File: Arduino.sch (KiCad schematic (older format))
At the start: 19 parts

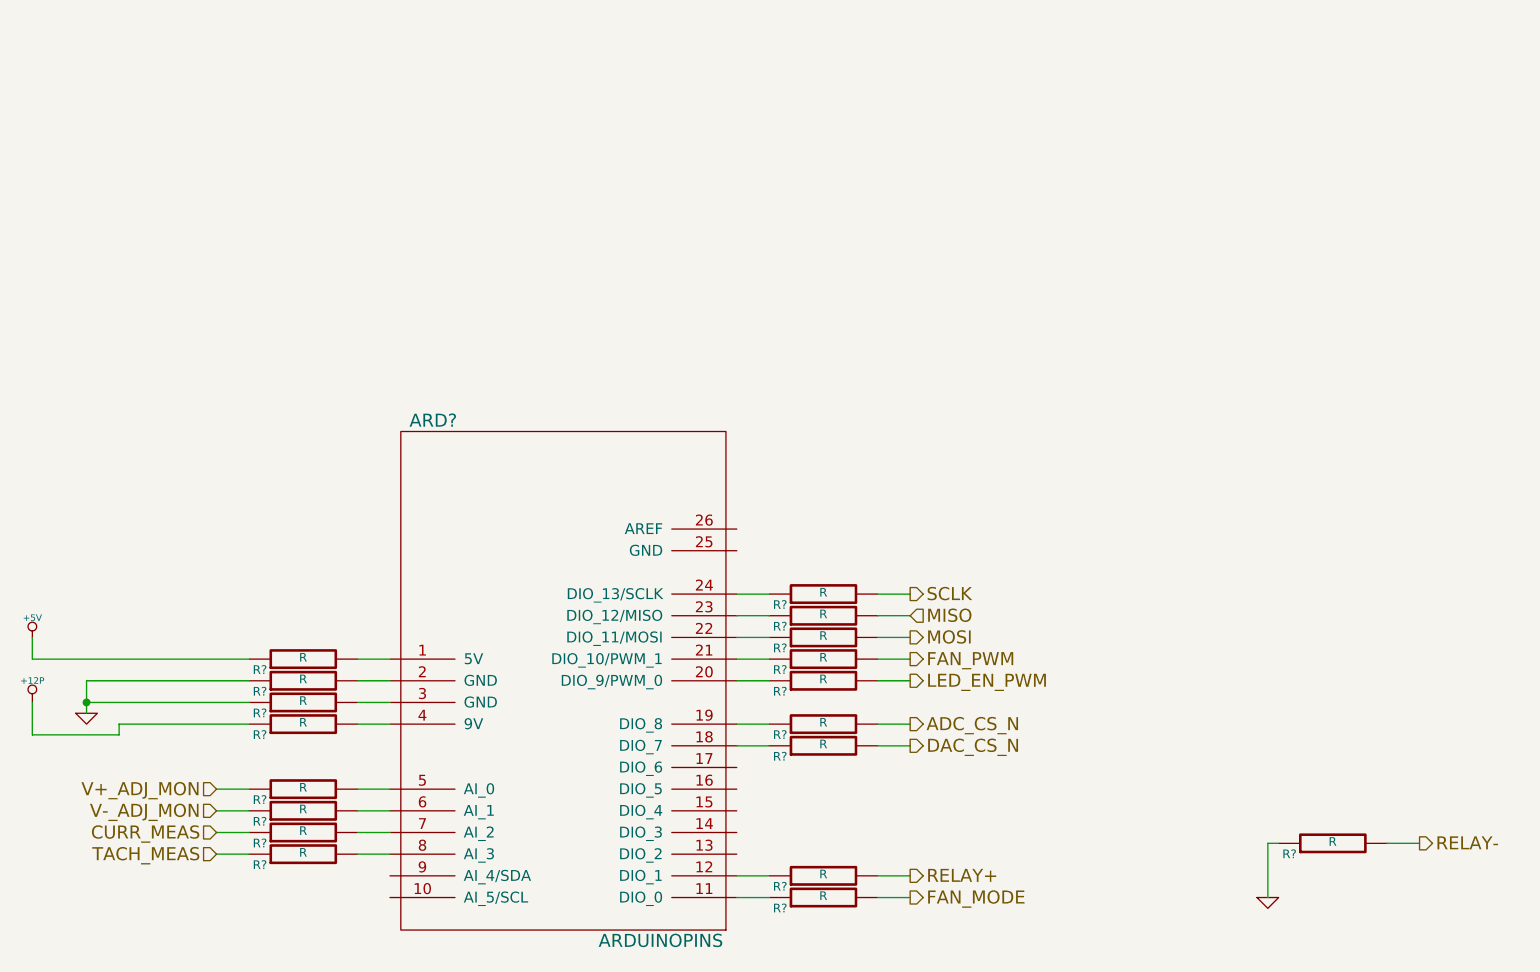
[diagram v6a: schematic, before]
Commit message: started associating relay parts
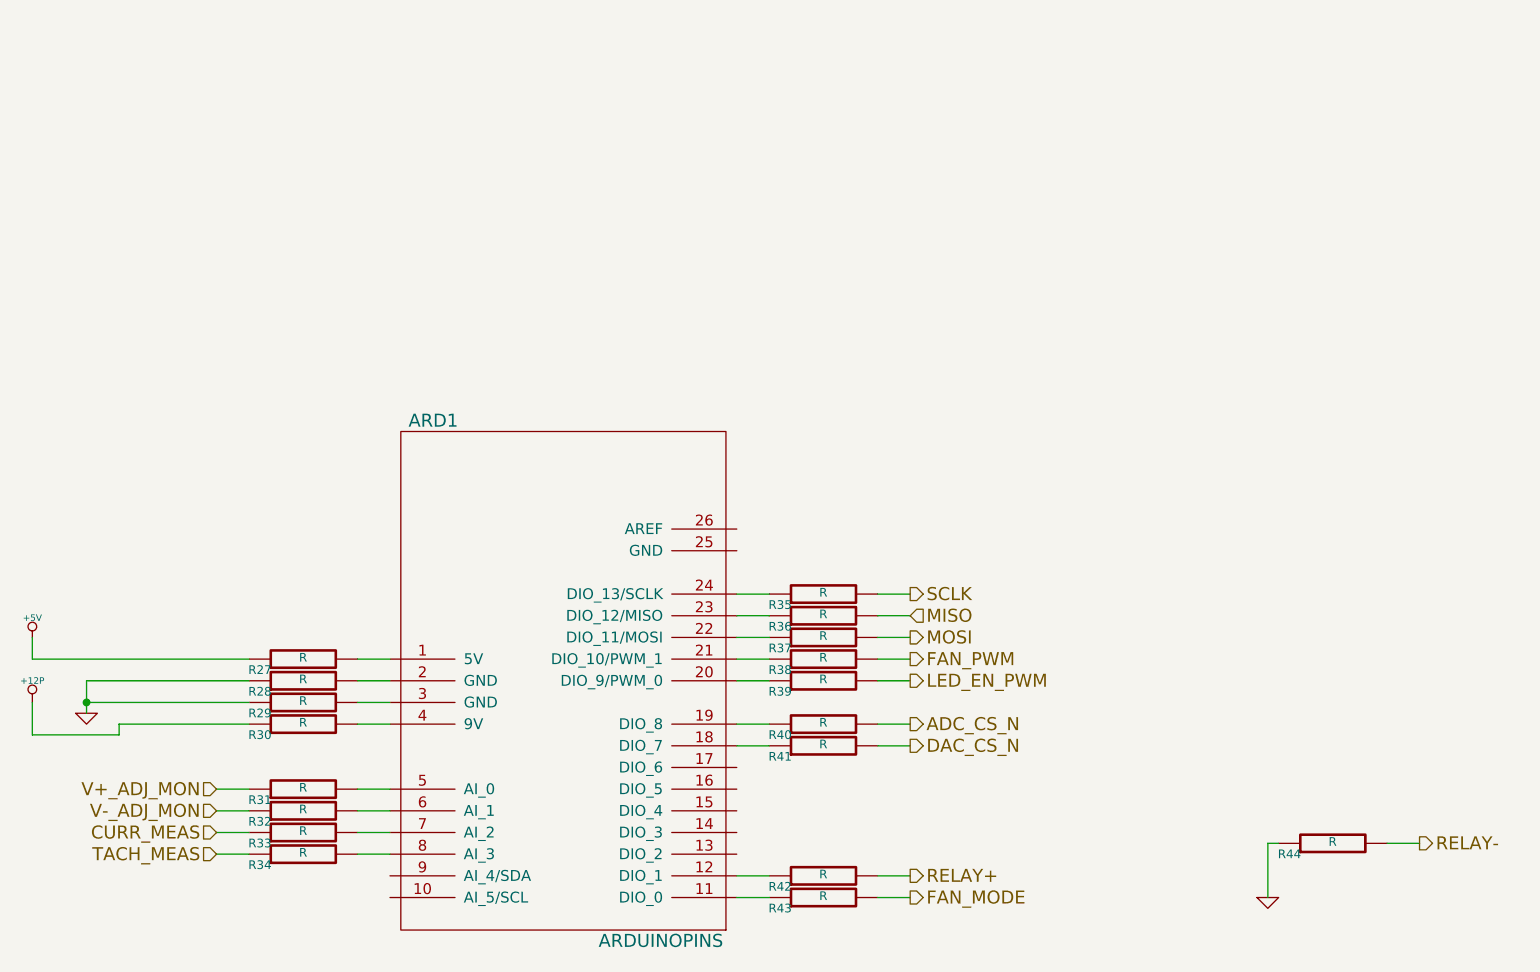
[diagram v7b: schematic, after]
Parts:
- gave numbers to parts that had none: 19
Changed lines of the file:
@@
 Sheet 9 9
 Title ""
-Date "17 feb 2014"
+Date "20 feb 2014"
 Rev ""
 Comp ""
@@
 CURR_MEAS
 $Comp
-L R R?
+L R R38
 U 1 1 52F9D91F
 P 6000 4300
-F 0 "R?" V 5950 4500 40  0000 C CNN
+F 0 "R38" V 5950 4500 40  0000 C CNN
 F 1 "R" V 6007 4301 40  0000 C CNN
 F 2 "~" V 5930 4300 30  0000 C CNN
@@
 $EndComp
 $Comp
-L R R?
+L R R42
 U 1 1 52F9E47A
 P 6000 5300
-F 0 "R?" V 5950 5500 40  0000 C CNN
+F 0 "R42" V 5950 5500 40  0000 C CNN
 F 1 "R" V 6007 5301 40  0000 C CNN
 F 2 "~" V 5930 5300 30  0000 C CNN
@@
 	5750 5300 5600 5300
 $Comp
-L GND #PWR?
+L GND #PWR049
 U 1 1 52F9E495
 P 8050 5400
-F 0 "#PWR?" H 8050 5400 30  0001 C CNN
+F 0 "#PWR049" H 8050 5400 30  0001 C CNN
 F 1 "GND" H 8050 5330 30  0001 C CNN
 F 2 "" H 8050 5400 60  0000 C CNN
@@
 $EndComp
 $Comp
-L R R?
+L R R34
 U 1 1 52FA0A84
 P 3600 5200
-F 0 "R?" V 3550 5400 40  0000 C CNN
+F 0 "R34" V 3550 5400 40  0000 C CNN
 F 1 "R" V 3607 5201 40  0000 C CNN
 F 2 "~" V 3530 5200 30  0000 C CNN
@@
 $EndComp
 $Comp
-L R R?
+L R R33
 U 1 1 52FA0A8A
 P 3600 5100
-F 0 "R?" V 3550 5300 40  0000 C CNN
+F 0 "R33" V 3550 5300 40  0000 C CNN
 F 1 "R" V 3607 5101 40  0000 C CNN
 F 2 "~" V 3530 5100 30  0000 C CNN
@@
 V-_ADJ_MON
 $Comp
-L R R?
+L R R32
 U 1 1 52FA4D64
 P 3600 5000
-F 0 "R?" V 3550 5200 40  0000 C CNN
+F 0 "R32" V 3550 5200 40  0000 C CNN
 F 1 "R" V 3607 5001 40  0000 C CNN
 F 2 "~" V 3530 5000 30  0000 C CNN
@@
 $EndComp
 $Comp
-L R R?
+L R R31
 U 1 1 52FA4D6A
 P 3600 4900
-F 0 "R?" V 3550 5100 40  0000 C CNN
+F 0 "R31" V 3550 5100 40  0000 C CNN
 F 1 "R" V 3607 4901 40  0000 C CNN
 F 2 "~" V 3530 4900 30  0000 C CNN
@@
 	3850 4900 4000 4900
 $Comp
-L R R?
+L R R44
 U 1 1 52FA5DED
 P 8350 5150
-F 0 "R?" V 8300 5350 40  0000 C CNN
+F 0 "R44" V 8300 5350 40  0000 C CNN
 F 1 "R" V 8357 5151 40  0000 C CNN
 F 2 "~" V 8280 5150 30  0000 C CNN
@@
 	8600 5150 8750 5150
 $Comp
-L R R?
+L R R41
 U 1 1 52FA6082
 P 6000 4700
-F 0 "R?" V 5950 4900 40  0000 C CNN
+F 0 "R41" V 5950 4900 40  0000 C CNN
 F 1 "R" V 6007 4701 40  0000 C CNN
 F 2 "~" V 5930 4700 30  0000 C CNN
@@
 $EndComp
 $Comp
-L R R?
+L R R37
 U 1 1 52FA6088
 P 6000 4200
-F 0 "R?" V 5950 4400 40  0000 C CNN
+F 0 "R37" V 5950 4400 40  0000 C CNN
 F 1 "R" V 6007 4201 40  0000 C CNN
 F 2 "~" V 5930 4200 30  0000 C CNN
@@
 $EndComp
 $Comp
-L R R?
+L R R36
 U 1 1 52FA608E
 P 6000 4100
-F 0 "R?" V 5950 4300 40  0000 C CNN
+F 0 "R36" V 5950 4300 40  0000 C CNN
 F 1 "R" V 6007 4101 40  0000 C CNN
 F 2 "~" V 5930 4100 30  0000 C CNN
@@
 $EndComp
 $Comp
-L R R?
+L R R35
 U 1 1 52FA6094
 P 6000 4000
-F 0 "R?" V 5950 4200 40  0000 C CNN
+F 0 "R35" V 5950 4200 40  0000 C CNN
 F 1 "R" V 6007 4001 40  0000 C CNN
 F 2 "~" V 5930 4000 30  0000 C CNN
@@
 LED_EN_PWM
 $Comp
-L R R?
+L R R39
 U 1 1 52FA63A1
 P 6000 4400
-F 0 "R?" V 5950 4600 40  0000 C CNN
+F 0 "R39" V 5950 4600 40  0000 C CNN
 F 1 "R" V 6007 4401 40  0000 C CNN
 F 2 "~" V 5930 4400 30  0000 C CNN
@@
 ADC_CS_N
 $Comp
-L R R?
+L R R40
 U 1 1 52FA944C
 P 6000 4600
-F 0 "R?" V 5950 4800 40  0000 C CNN
+F 0 "R40" V 5950 4800 40  0000 C CNN
 F 1 "R" V 6007 4601 40  0000 C CNN
 F 2 "~" V 5930 4600 30  0000 C CNN
@@
 FAN_MODE
 $Comp
-L R R?
+L R R43
 U 1 1 52FA55B0
 P 6000 5400
-F 0 "R?" V 5950 5600 40  0000 C CNN
+F 0 "R43" V 5950 5600 40  0000 C CNN
 F 1 "R" V 6007 5401 40  0000 C CNN
 F 2 "~" V 5930 5400 30  0000 C CNN
@@
 	6250 5400 6400 5400
 $Comp
-L R R?
+L R R30
 U 1 1 52FA5B06
 P 3600 4600
-F 0 "R?" V 3550 4800 40  0000 C CNN
+F 0 "R30" V 3550 4800 40  0000 C CNN
 F 1 "R" V 3607 4601 40  0000 C CNN
 F 2 "~" V 3530 4600 30  0000 C CNN
@@
 	3850 4600 4000 4600
 $Comp
-L +12P #PWR?
+L +12P #PWR050
 U 1 1 52FA5B4B
 P 2350 4500
-F 0 "#PWR?" H 2350 4470 30  0001 C CNN
+F 0 "#PWR050" H 2350 4470 30  0001 C CNN
 F 1 "+12P" H 2350 4600 30  0000 C CNN
 F 2 "" H 2350 4500 60  0000 C CNN
@@
 	2350 4500 2350 4650
 $Comp
-L ARDUINOPINS ARD?
+L ARDUINOPINS ARD1
 U 1 1 53022634
 P 6350 4700
-F 0 "ARD?" H 4200 6200 60  0000 C CNN
+F 0 "ARD1" H 4200 6200 60  0000 C CNN
 F 1 "ARDUINOPINS" H 5250 3800 60  0000 C CNN
 F 2 "~" H 6350 4700 60  0000 C CNN
@@
 $EndComp
 $Comp
-L R R?
+L R R27
 U 1 1 53023A69
 P 3600 4300
-F 0 "R?" V 3550 4500 40  0000 C CNN
+F 0 "R27" V 3550 4500 40  0000 C CNN
 F 1 "R" V 3607 4301 40  0000 C CNN
 F 2 "~" V 3530 4300 30  0000 C CNN
@@
 $EndComp
 $Comp
-L R R?
+L R R28
 U 1 1 53023A6F
 P 3600 4400
-F 0 "R?" V 3550 4600 40  0000 C CNN
+F 0 "R28" V 3550 4600 40  0000 C CNN
 F 1 "R" V 3607 4401 40  0000 C CNN
 F 2 "~" V 3530 4400 30  0000 C CNN
@@
 $EndComp
 $Comp
-L R R?
+L R R29
 U 1 1 53023A7F
 P 3600 4500
-F 0 "R?" V 3550 4700 40  0000 C CNN
+F 0 "R29" V 3550 4700 40  0000 C CNN
 F 1 "R" V 3607 4501 40  0000 C CNN
 F 2 "~" V 3530 4500 30  0000 C CNN
@@
 	3850 4300 4000 4300
 $Comp
-L +5V #PWR?
+L +5V #PWR051
 U 1 1 53023B11
 P 2350 4200
-F 0 "#PWR?" H 2350 4290 20  0001 C CNN
+F 0 "#PWR051" H 2350 4290 20  0001 C CNN
 F 1 "+5V" H 2350 4290 30  0000 C CNN
 F 2 "" H 2350 4200 60  0000 C CNN
@@
 	2350 4300 3350 4300
 $Comp
-L GND #PWR?
+L GND #PWR052
 U 1 1 53023B7D
 P 2600 4550
-F 0 "#PWR?" H 2600 4550 30  0001 C CNN
+F 0 "#PWR052" H 2600 4550 30  0001 C CNN
 F 1 "GND" H 2600 4480 30  0001 C CNN
 F 2 "" H 2600 4550 60  0000 C CNN

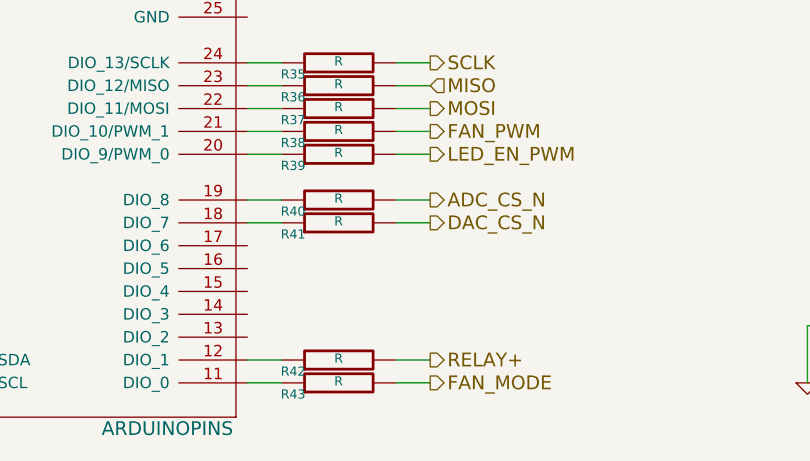
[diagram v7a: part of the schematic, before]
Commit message: worked on associating parts
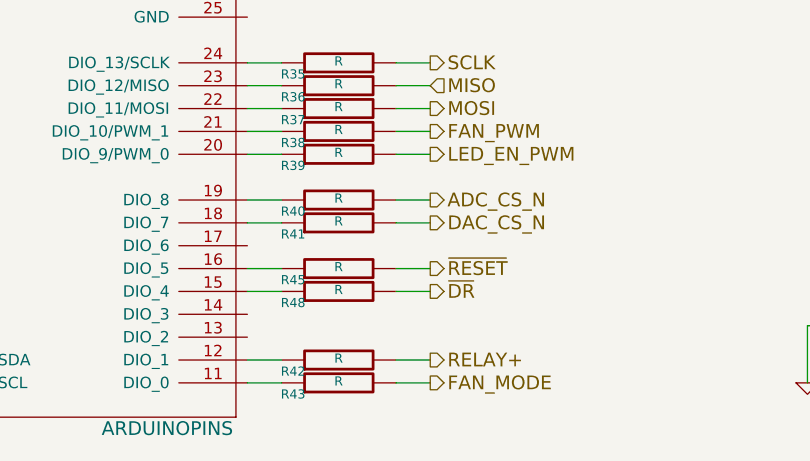
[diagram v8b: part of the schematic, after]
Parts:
- added R45, R48: R, ~, symbol R
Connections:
- net at ARD1.15 (DIO_4): now also R48.1
- net at ARD1.16 (DIO_5): now also R45.1
- new net ~DR: R48.2
- new net ~RESET: R45.2
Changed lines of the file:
@@
 Sheet 9 9
 Title ""
-Date "20 feb 2014"
+Date "23 feb 2014"
 Rev ""
 Comp ""
@@
 	5750 5300 5600 5300
 $Comp
-L GND #PWR049
+L GND #PWR65
 U 1 1 52F9E495
 P 8050 5400
-F 0 "#PWR049" H 8050 5400 30  0001 C CNN
+F 0 "#PWR65" H 8050 5400 30  0001 C CNN
 F 1 "GND" H 8050 5330 30  0001 C CNN
 F 2 "" H 8050 5400 60  0000 C CNN
@@
 	3850 4600 4000 4600
 $Comp
-L +12P #PWR050
+L +12P #PWR63
 U 1 1 52FA5B4B
 P 2350 4500
-F 0 "#PWR050" H 2350 4470 30  0001 C CNN
+F 0 "#PWR63" H 2350 4470 30  0001 C CNN
 F 1 "+12P" H 2350 4600 30  0000 C CNN
 F 2 "" H 2350 4500 60  0000 C CNN
@@
 	3850 4300 4000 4300
 $Comp
-L +5V #PWR051
+L +5V #PWR62
 U 1 1 53023B11
 P 2350 4200
-F 0 "#PWR051" H 2350 4290 20  0001 C CNN
+F 0 "#PWR62" H 2350 4290 20  0001 C CNN
 F 1 "+5V" H 2350 4290 30  0000 C CNN
 F 2 "" H 2350 4200 60  0000 C CNN
@@
 	2350 4300 3350 4300
 $Comp
-L GND #PWR052
+L GND #PWR64
 U 1 1 53023B7D
 P 2600 4550
-F 0 "#PWR052" H 2600 4550 30  0001 C CNN
+F 0 "#PWR64" H 2600 4550 30  0001 C CNN
 F 1 "GND" H 2600 4480 30  0001 C CNN
 F 2 "" H 2600 4550 60  0000 C CNN
@@
 Wire Wire Line
 	2750 4650 2350 4650
+$Comp
+L R R45
+U 1 1 530A88BC
+P 6000 4900
+F 0 "R45" V 5950 5100 40  0000 C CNN
+F 1 "R" V 6007 4901 40  0000 C CNN
+F 2 "~" V 5930 4900 30  0000 C CNN
+F 3 "~" H 6000 4900 30  0000 C CNN
+	1    6000 4900
+	0    -1   -1   0
+$EndComp
+$Comp
+L R R48
+U 1 1 530A88C8
+P 6000 5000
+F 0 "R48" V 5950 5200 40  0000 C CNN
+F 1 "R" V 6007 5001 40  0000 C CNN
+F 2 "~" V 5930 5000 30  0000 C CNN
+F 3 "~" H 6000 5000 30  0000 C CNN
+	1    6000 5000
+	0    -1   -1   0
+$EndComp
+Text HLabel 6400 4900 2    60   Output ~ 0
+~RESET
+Text HLabel 6400 5000 2    60   Output ~ 0
+~DR
+Wire Wire Line
+	6250 5000 6400 5000
+Wire Wire Line
+	6250 4900 6400 4900
+Wire Wire Line
+	5750 4900 5600 4900
+Wire Wire Line
+	5750 5000 5600 5000
 $EndSCHEMATC
